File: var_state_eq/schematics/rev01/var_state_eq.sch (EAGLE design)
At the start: 69 parts, among them IC1 TL084P, IC2 TL084P, IC3 TL084P, J1 IN, J2 OUT

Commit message: EQ schem review
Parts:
- R11, R22: value 100K -> 5.1K
- R15, R6: value 10K -> 20K
- R16, R8: value 20K -> 5.1K
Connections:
- new net N$40: IC2A.+IN, R11.2, R12.1
- net +12V: now also JP1.10, JP1.9; no longer JP1.1, JP1.2
- net -12V: now also JP1.1, JP1.2; no longer JP1.10, JP1.9
- net 0V: no longer IC2A.+IN, R11.2, R12.1
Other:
- note added: "Using LOG (A) pots, instead of -LOG (C); wired so freq will increase CCW."
- note removed: "Note using LOG (A) pots, instead of -LOG (C), and wired so freq will increase CCW."
- moved on the sheet: C12, C13, C14, C20, C21, C23, C24, IC2A, IC2B, IC2C, JP1, R11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

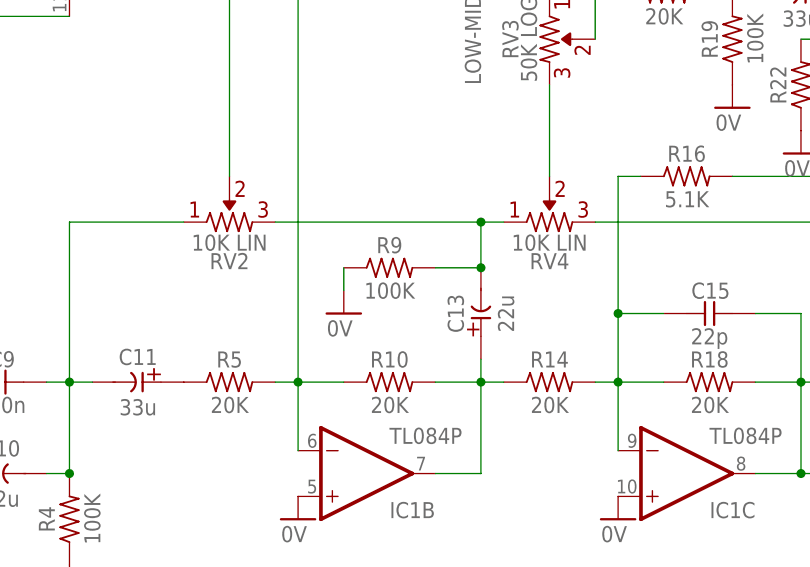
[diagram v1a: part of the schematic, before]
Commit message: Updated EQ labels
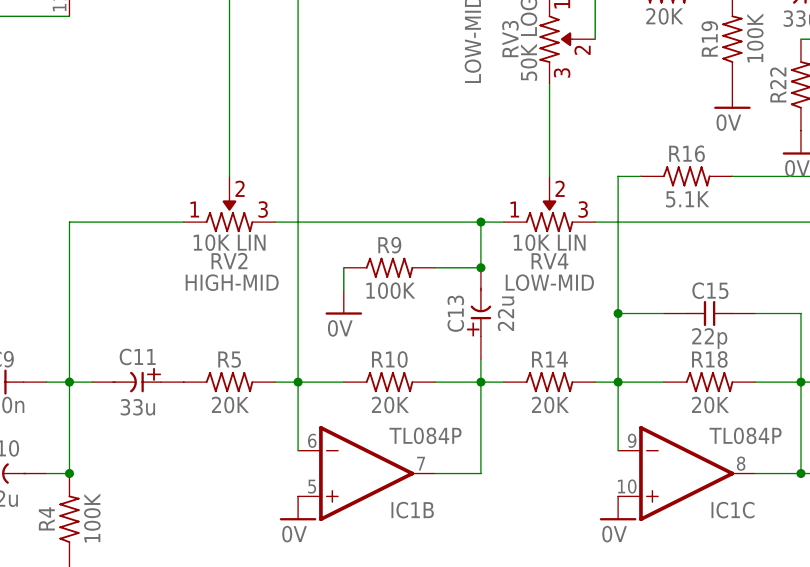
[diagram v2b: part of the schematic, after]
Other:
- note added: "HIGH-MID"
- note added: "LOW-MID"
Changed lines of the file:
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@@
 <?xml version="1.0" encoding="utf-8"?>
 <!DOCTYPE eagle SYSTEM "eagle.dtd">
-<eagle version="9.5.1">
+<eagle version="9.5.2">
 <drawing>
 <settings>
@@
 <text x="208.28" y="147.32" size="1.778" layer="97">LOW MID FREQ</text>
 <text x="195.58" y="160.02" size="1.778" layer="97">Using LOG (A) pots, instead of -LOG (C); wired so freq will increase CCW.</text>
+<text x="83.82" y="101.6" size="1.778" layer="96">HIGH-MID</text>
+<text x="119.38" y="101.6" size="1.778" layer="96">LOW-MID</text>
 </plain>
 <instances>

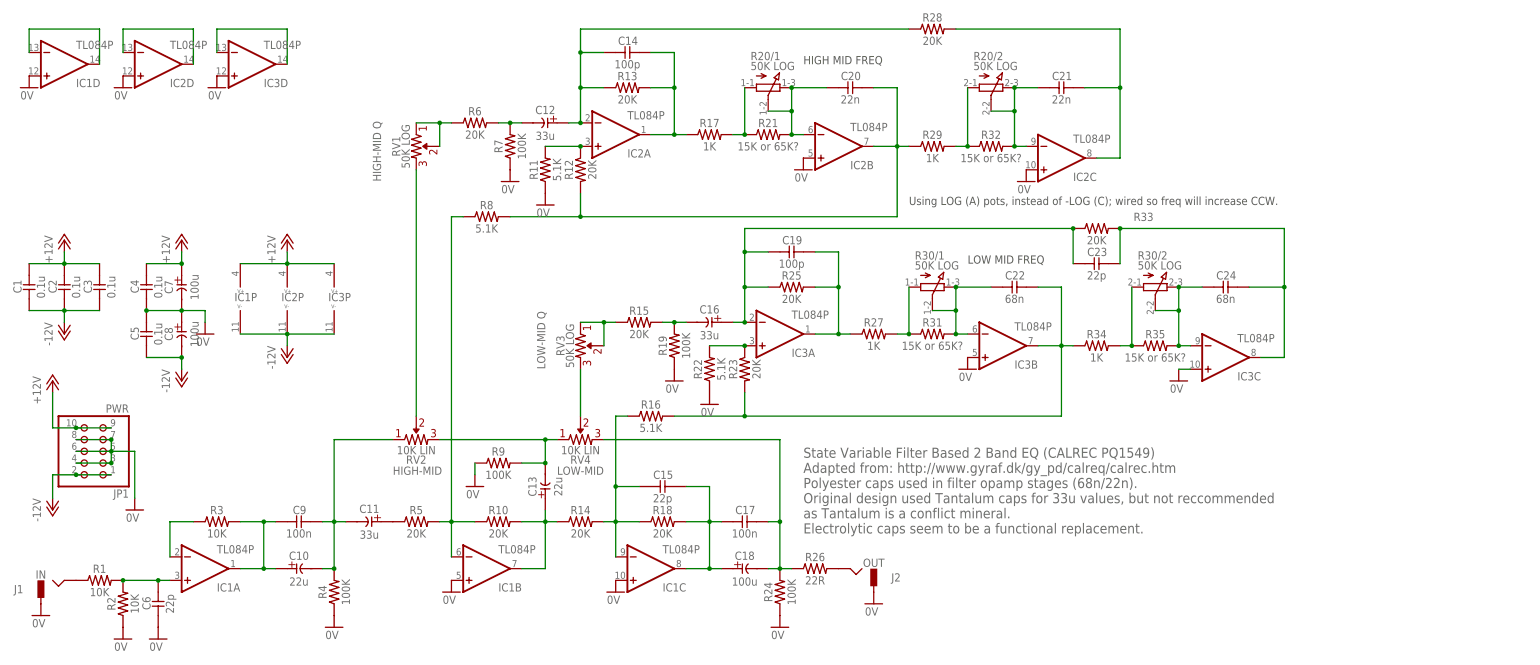
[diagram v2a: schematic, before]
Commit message: Updated EQ with as-build values
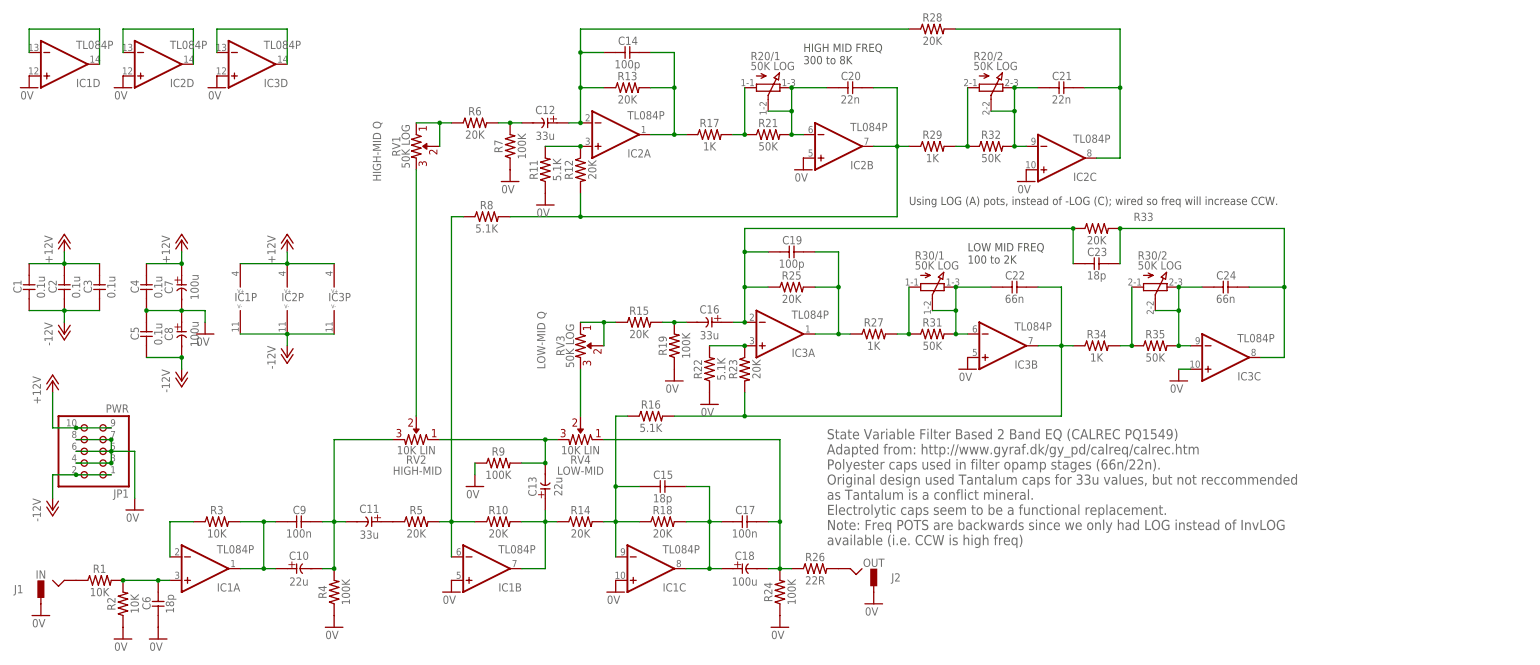
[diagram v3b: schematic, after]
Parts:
- C15, C23, C6: value 22p -> 18p
- C22, C24: value 68n -> 66n
- R21, R31, R32, R35: value 15K or 65K? -> 50K
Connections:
- net N$16: now also RV4.1; no longer RV4.2
- net N$7: now also RV2.1, RV4.2; no longer RV2.2, RV4.1
- net N$8: now also RV2.2; no longer RV2.1
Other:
- note added: "HIGH MID FREQ 300 to 8K"
- note added: "LOW MID FREQ 100 to 2K"
- note added: "State Variable Filter Based 2 Band EQ (CALREC PQ1549) Adapted from: http://www.gyraf.dk/gy_pd/calreq/calrec.htm Polyester caps used in filter opamp stages (66n/22n). Original design used Tantalum caps for 33u values, but not reccommended as Tantalum is a conflict mineral. Electrolytic caps seem to be a functional replacement. Note: Freq POTS are backwards since we only had LOG instead of InvLOG a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"
- note removed: "HIGH MID FREQ"
- note removed: "LOW MID FREQ"
- note removed: "State Variable Filter Based 2 Band EQ (CALREC PQ1549) Adapted from: http://www.gyraf.dk/gy_pd/calreq/calrec.htm Polyester caps used in filter opamp stages (68n/22n). Original design used Tantalum caps for 33u values, but not reccommended as Tantalum is a conflict mineral. Electrolytic caps seem to be a functional replacement."

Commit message: Added routed board; switched to film caps
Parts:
- C18: device _common:CE-USE2-5 -> _common:CE-USE5-8.5
- C20, C21: device _common:CC-US025-024X044 -> _common:CC-US050-024X044
- C22, C24: value 66n -> 68n; device _common:CC-US025-024X044 -> _common:CC-US050-024X044
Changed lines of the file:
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@@
 <?xml version="1.0" encoding="utf-8"?>
 <!DOCTYPE eagle SYSTEM "eagle.dtd">
-<eagle version="9.5.1">
+<eagle version="9.6.1">
 <drawing>
 <settings>
@@
 <layer number="18" name="Vias" color="2" fill="1" visible="yes" active="no"/>
 <layer number="19" name="Unrouted" color="6" fill="1" visible="yes" active="no"/>
-<layer number="20" name="Dimension" color="15" fill="1" visible="yes" active="no"/>
+<layer number="20" name="Dimension" color="24" fill="1" visible="yes" active="no"/>
 <layer number="21" name="tPlace" color="7" fill="1" visible="yes" active="no"/>
 <layer number="22" name="bPlace" color="7" fill="1" visible="yes" active="no"/>
@@
 <part name="C15" library="_common" deviceset="CC-US" device="025-024X044" value="18p"/>
 <part name="C17" library="_common" deviceset="CC-US" device="025-024X044" value="100n"/>
-<part name="C18" library="_common" deviceset="CE-US" device="E2-5" value="100u"/>
+<part name="C18" library="_common" deviceset="CE-US" device="E5-8.5" value="100u"/>
 <part name="R26" library="_common" deviceset="R" device="" value="22R"/>
 <part name="R24" library="_common" deviceset="R" device="" value="100K"/>
@@
 <part name="GND17" library="supply1" library_urn="urn:adsk.eagle:library:371" deviceset="0V" device=""/>
 <part name="R12" library="_common" deviceset="R" device="" value="20K"/>
-<part name="C20" library="_common" deviceset="CC-US" device="025-024X044" value="22n"/>
+<part name="C20" library="_common" deviceset="CC-US" device="050-024X044" value="22n"/>
 <part name="R29" library="_common" deviceset="R" device="" value="1K"/>
 <part name="R32" library="_common" deviceset="R" device="" value="50K"/>
-<part name="C21" library="_common" deviceset="CC-US" device="025-024X044" value="22n"/>
+<part name="C21" library="_common" deviceset="CC-US" device="050-024X044" value="22n"/>
 <part name="GND21" library="supply1" library_urn="urn:adsk.eagle:library:371" deviceset="0V" device=""/>
 <part name="R28" library="_common" deviceset="R" device="" value="20K"/>
@@
 <part name="R31" library="_common" deviceset="R" device="" value="50K"/>
 <part name="R30" library="_common" deviceset="3RP/1610G" device="" package3d_urn="urn:adsk.eagle:package:22728/1" value="50K LOG"/>
-<part name="C22" library="_common" deviceset="CC-US" device="025-024X044" value="66n"/>
-<part name="C24" library="_common" deviceset="CC-US" device="025-024X044" value="66n"/>
+<part name="C22" library="_common" deviceset="CC-US" device="050-024X044" value="68n"/>
+<part name="C24" library="_common" deviceset="CC-US" device="050-024X044" value="68n"/>
 <part name="R34" library="_common" deviceset="R" device="" value="1K"/>
 <part name="R35" library="_common" deviceset="R" device="" value="50K"/>
@@
 </segment>
 </net>
-<net name="N$40" class="1">
+<net name="N$40" class="0">
 <segment>
 <pinref part="R11" gate="G$1" pin="2"/>

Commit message: Updates for part purchase
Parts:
- R26: value 22R -> 100R
- R31, R35: value 50K -> 56K
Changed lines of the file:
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@@
 <?xml version="1.0" encoding="utf-8"?>
 <!DOCTYPE eagle SYSTEM "eagle.dtd">
-<eagle version="9.6.1">
+<eagle version="9.5.1">
 <drawing>
 <settings>
@@
 <grid distance="0.1" unitdist="inch" unit="inch" style="lines" multiple="1" display="no" altdistance="0.01" altunitdist="inch" altunit="inch"/>
 <layers>
-<layer number="1" name="Top" color="4" fill="1" visible="yes" active="no"/>
-<layer number="16" name="Bottom" color="1" fill="1" visible="yes" active="no"/>
-<layer number="17" name="Pads" color="2" fill="1" visible="yes" active="no"/>
-<layer number="18" name="Vias" color="2" fill="1" visible="yes" active="no"/>
-<layer number="19" name="Unrouted" color="6" fill="1" visible="yes" active="no"/>
-<layer number="20" name="Dimension" color="24" fill="1" visible="yes" active="no"/>
-<layer number="21" name="tPlace" color="7" fill="1" visible="yes" active="no"/>
-<layer number="22" name="bPlace" color="7" fill="1" visible="yes" active="no"/>
-<layer number="23" name="tOrigins" color="15" fill="1" visible="yes" active="no"/>
-<layer number="24" name="bOrigins" color="15" fill="1" visible="yes" active="no"/>
-<layer number="25" name="tNames" color="7" fill="1" visible="yes" active="no"/>
-<layer number="26" name="bNames" color="7" fill="1" visible="yes" active="no"/>
-<layer number="27" name="tValues" color="7" fill="1" visible="yes" active="no"/>
-<layer number="28" name="bValues" color="7" fill="1" visible="yes" active="no"/>
+<layer number="1" name="Top" color="4" fill="1" visible="no" active="no"/>
+<layer number="16" name="Bottom" color="1" fill="1" visible="no" active="no"/>
+<layer number="17" name="Pads" color="2" fill="1" visible="no" active="no"/>
+<layer number="18" name="Vias" color="2" fill="1" visible="no" active="no"/>
+<layer number="19" name="Unrouted" color="6" fill="1" visible="no" active="no"/>
+<layer number="20" name="Dimension" color="24" fill="1" visible="no" active="no"/>
+<layer number="21" name="tPlace" color="7" fill="1" visible="no" active="no"/>
+<layer number="22" name="bPlace" color="7" fill="1" visible="no" active="no"/>
+<layer number="23" name="tOrigins" color="15" fill="1" visible="no" active="no"/>
+<layer number="24" name="bOrigins" color="15" fill="1" visible="no" active="no"/>
+<layer number="25" name="tNames" color="7" fill="1" visible="no" active="no"/>
+<layer number="26" name="bNames" color="7" fill="1" visible="no" active="no"/>
+<layer number="27" name="tValues" color="7" fill="1" visible="no" active="no"/>
+<layer number="28" name="bValues" color="7" fill="1" visible="no" active="no"/>
 <layer number="29" name="tStop" color="7" fill="3" visible="no" active="no"/>
 <layer number="30" name="bStop" color="7" fill="6" visible="no" active="no"/>
@@
 <layer number="35" name="tGlue" color="7" fill="4" visible="no" active="no"/>
 <layer number="36" name="bGlue" color="7" fill="5" visible="no" active="no"/>
-<layer number="37" name="tTest" color="7" fill="1" visible="yes" active="no"/>
-<layer number="38" name="bTest" color="7" fill="1" visible="yes" active="no"/>
+<layer number="37" name="tTest" color="7" fill="1" visible="no" active="no"/>
+<layer number="38" name="bTest" color="7" fill="1" visible="no" active="no"/>
 <layer number="39" name="tKeepout" color="4" fill="11" visible="no" active="no"/>
 <layer number="40" name="bKeepout" color="1" fill="11" visible="no" active="no"/>
@@
 <layer number="44" name="Drills" color="7" fill="1" visible="no" active="no"/>
 <layer number="45" name="Holes" color="7" fill="1" visible="no" active="no"/>
-<layer number="46" name="Milling" color="3" fill="1" visible="yes" active="no"/>
-<layer number="47" name="Measures" color="7" fill="1" visible="yes" active="no"/>
-<layer number="48" name="Document" color="7" fill="1" visible="yes" active="no"/>
-<layer number="49" name="Reference" color="7" fill="1" visible="yes" active="no"/>
-<layer number="50" name="dxf" color="7" fill="1" visible="yes" active="no"/>
-<layer number="51" name="tDocu" color="7" fill="1" visible="yes" active="no"/>
-<layer number="52" name="bDocu" color="7" fill="1" visible="yes" active="no"/>
+<layer number="46" name="Milling" color="3" fill="1" visible="no" active="no"/>
+<layer number="47" name="Measures" color="7" fill="1" visible="no" active="no"/>
+<layer number="48" name="Document" color="7" fill="1" visible="no" active="no"/>
+<layer number="49" name="Reference" color="7" fill="1" visible="no" active="no"/>
+<layer number="50" name="dxf" color="7" fill="1" visible="no" active="no"/>
+<layer number="51" name="tDocu" color="7" fill="1" visible="no" active="no"/>
+<layer number="52" name="bDocu" color="7" fill="1" visible="no" active="no"/>
 <layer number="88" name="SimResults" color="9" fill="1" visible="yes" active="yes"/>
 <layer number="89" name="SimProbes" color="9" fill="1" visible="yes" active="yes"/>
@@
 <part name="C17" library="_common" deviceset="CC-US" device="025-024X044" value="100n"/>
 <part name="C18" library="_common" deviceset="CE-US" device="E5-8.5" value="100u"/>
-<part name="R26" library="_common" deviceset="R" device="" value="22R"/>
+<part name="R26" library="_common" deviceset="R" device="" value="100R"/>
 <part name="R24" library="_common" deviceset="R" device="" value="100K"/>
 <part name="GND2" library="supply1" library_urn="urn:adsk.eagle:library:371" deviceset="0V" device=""/>
@@
 <part name="C19" library="_common" deviceset="CC-US" device="025-024X044" value="100p"/>
 <part name="R27" library="_common" deviceset="R" device="" value="1K"/>
-<part name="R31" library="_common" deviceset="R" device="" value="50K"/>
+<part name="R31" library="_common" deviceset="R" device="" value="56K"/>
 <part name="R30" library="_common" deviceset="3RP/1610G" device="" package3d_urn="urn:adsk.eagle:package:22728/1" value="50K LOG"/>
 <part name="C22" library="_common" deviceset="CC-US" device="050-024X044" value="68n"/>
 <part name="C24" library="_common" deviceset="CC-US" device="050-024X044" value="68n"/>
 <part name="R34" library="_common" deviceset="R" device="" value="1K"/>
-<part name="R35" library="_common" deviceset="R" device="" value="50K"/>
+<part name="R35" library="_common" deviceset="R" device="" value="56K"/>
 <part name="R33" library="_common" deviceset="R" device="" value="20K"/>
 <part name="C23" library="_common" deviceset="CC-US" device="025-024X044" value="18p"/>

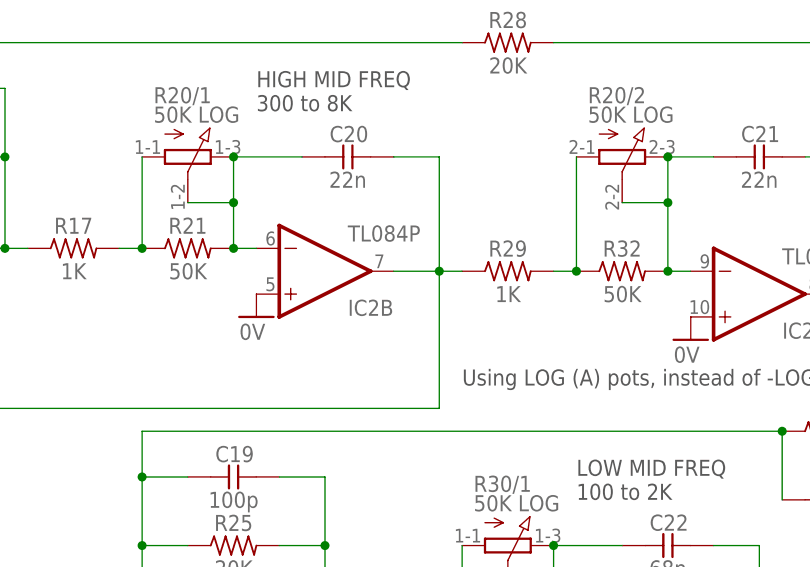
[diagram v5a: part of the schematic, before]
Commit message: Updated resistor values to 56K
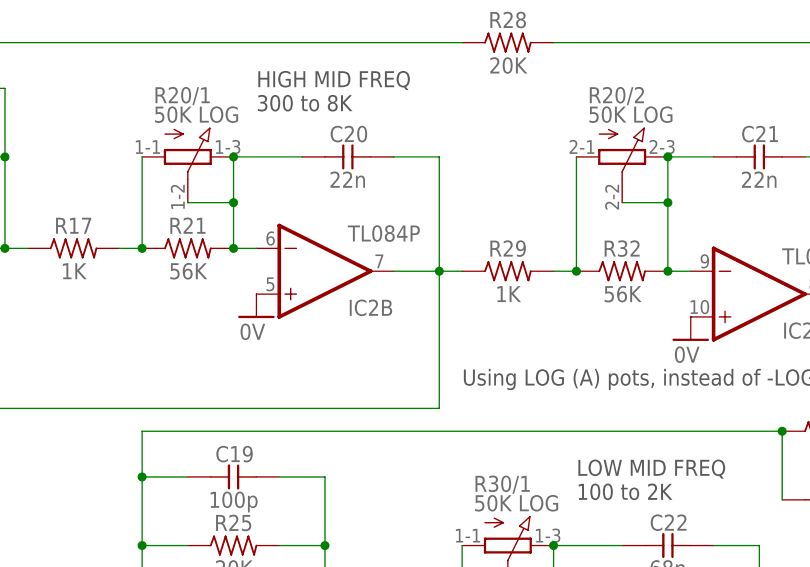
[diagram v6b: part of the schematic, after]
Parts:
- R21, R32: value 50K -> 56K
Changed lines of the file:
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@@
 <?xml version="1.0" encoding="utf-8"?>
 <!DOCTYPE eagle SYSTEM "eagle.dtd">
-<eagle version="9.5.1">
+<eagle version="9.5.2">
 <drawing>
 <settings>
@@
 <part name="C14" library="_common" deviceset="CC-US" device="025-024X044" value="100p"/>
 <part name="R17" library="_common" deviceset="R" device="" value="1K"/>
-<part name="R21" library="_common" deviceset="R" device="" value="50K"/>
+<part name="R21" library="_common" deviceset="R" device="" value="56K"/>
 <part name="R20" library="_common" deviceset="3RP/1610G" device="" package3d_urn="urn:adsk.eagle:package:22728/1" value="50K LOG"/>
 <part name="GND17" library="supply1" library_urn="urn:adsk.eagle:library:371" deviceset="0V" device=""/>
@@
 <part name="C20" library="_common" deviceset="CC-US" device="050-024X044" value="22n"/>
 <part name="R29" library="_common" deviceset="R" device="" value="1K"/>
-<part name="R32" library="_common" deviceset="R" device="" value="50K"/>
+<part name="R32" library="_common" deviceset="R" device="" value="56K"/>
 <part name="C21" library="_common" deviceset="CC-US" device="050-024X044" value="22n"/>
 <part name="GND21" library="supply1" library_urn="urn:adsk.eagle:library:371" deviceset="0V" device=""/>
